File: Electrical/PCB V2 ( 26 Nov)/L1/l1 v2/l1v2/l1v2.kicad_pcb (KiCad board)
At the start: 2 copper layers, 177.9 x 169.6 mm, 157 parts, among them J1 Conn_01x01_Socket, J2 Conn_01x01_Socket, SW1 SW_SPDT, U1 ESP32-WROOM-32D-N4, U2 CD74HC4067SM, U3 CD74HC4067SM

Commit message: unfinished ocb with parts list
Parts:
- removed C22: 1uF, Capacitor_SMD:C_0603_1608Metric
- added C63: 1uF, Capacitor_SMD:C_0603_1608Metric, F.Cu at (164.0, 138.7)
- added L1: 10µH, Inductor_SMD:L_0805_2012Metric, F.Cu at (165.5, 116.1)
- added L33: 10µH, Inductor_SMD:L_0805_2012Metric, F.Cu at (166.1, 106.1)
- added L34: 10µH, Inductor_SMD:L_0805_2012Metric, F.Cu at (164.7, 96.2)
- added L35: 10µH, Inductor_SMD:L_0805_2012Metric, F.Cu at (161.4, 86.8)
- added L36: 10µH, Inductor_SMD:L_0805_2012Metric, F.Cu at (156.4, 78.2)
- added L37: 10µH, Inductor_SMD:L_0805_2012Metric, F.Cu at (149.7, 70.7)
- added L38: 10µH, Inductor_SMD:L_0805_2012Metric, F.Cu at (141.8, 64.7)
- added L39: 10µH, Inductor_SMD:L_0805_2012Metric, F.Cu at (132.8, 60.3)
- added L40: 10µH, Inductor_SMD:L_0805_2012Metric, F.Cu at (123.1, 57.8)
- added L41: 10µH, Inductor_SMD:L_0805_2012Metric, F.Cu at (113.1, 57.2)
- added L42: 10µH, Inductor_SMD:L_0805_2012Metric, F.Cu at (103.2, 58.6)
- added L43: 10µH, Inductor_SMD:L_0805_2012Metric, F.Cu at (93.8, 61.8)
- added L44: 10µH, Inductor_SMD:L_0805_2012Metric, F.Cu at (85.1, 66.9)
- added L45: 10µH, Inductor_SMD:L_0805_2012Metric, F.Cu at (77.7, 73.5)
- added L46: 10µH, Inductor_SMD:L_0805_2012Metric, F.Cu at (71.6, 81.5)
- added L47: 10µH, Inductor_SMD:L_0805_2012Metric, F.Cu at (67.3, 90.5)
- added L48: 10µH, Inductor_SMD:L_0805_2012Metric, F.Cu at (64.7, 100.2)
- added L49: 10µH, Inductor_SMD:L_0805_2012Metric, F.Cu at (64.2, 110.1)
- added L50: 10µH, Inductor_SMD:L_0805_2012Metric, F.Cu at (65.5, 120.0)
- added L51: 10µH, Inductor_SMD:L_0805_2012Metric, F.Cu at (68.8, 129.5)
- added L52: 10µH, Inductor_SMD:L_0805_2012Metric, F.Cu at (73.9, 138.1)
- added L53: 10µH, Inductor_SMD:L_0805_2012Metric, F.Cu at (80.5, 145.6)
- added L54: 10µH, Inductor_SMD:L_0805_2012Metric, F.Cu at (88.5, 151.6)
- added L55: 10µH, Inductor_SMD:L_0805_2012Metric, F.Cu at (97.5, 156.0)
- added L56: 10µH, Inductor_SMD:L_0805_2012Metric, F.Cu at (107.1, 158.5)
- added L57: 10µH, Inductor_SMD:L_0805_2012Metric, F.Cu at (117.1, 159.1)
- added L58: 10µH, Inductor_SMD:L_0805_2012Metric, F.Cu at (127.0, 157.7)
- added L59: 10µH, Inductor_SMD:L_0805_2012Metric, F.Cu at (136.5, 154.5)
- added L60: 10µH, Inductor_SMD:L_0805_2012Metric, F.Cu at (145.1, 149.4)
- added L61: 10µH, Inductor_SMD:L_0805_2012Metric, F.Cu at (152.6, 142.8)
- added L62: 10µH, Inductor_SMD:L_0805_2012Metric, F.Cu at (158.6, 134.8)
- added L63: 10µH, Inductor_SMD:L_0805_2012Metric, F.Cu at (163.0, 125.8)
- added LED10: WHITE 3528, LED_SMD:LED_PLCC_2835, F.Cu at (275.1, 145.3)
- added LED11: WHITE 3528, LED_SMD:LED_PLCC_2835, F.Cu at (264.8, 138.9)
- added LED12: WHITE 3528, LED_SMD:LED_PLCC_2835, F.Cu at (264.8, 140.6)
- added LED13: WHITE 3528, LED_SMD:LED_PLCC_2835, F.Cu at (264.8, 142.4)
- added LED14: WHITE 3528, LED_SMD:LED_PLCC_2835, F.Cu at (264.8, 144.1)
- added LED15: WHITE 3528, LED_SMD:LED_PLCC_2835, F.Cu at (264.8, 145.9)
- added LED16: WHITE 3528, LED_SMD:LED_PLCC_2835, F.Cu at (264.8, 147.6)
- added LED17: WHITE 3528, LED_SMD:LED_PLCC_2835, F.Cu at (264.8, 149.4)
- added LED18: WHITE 3528, LED_SMD:LED_PLCC_2835, F.Cu at (264.8, 151.1)
- added LED19: WHITE 3528, LED_SMD:LED_PLCC_2835, F.Cu at (267.5, 137.1)
- added LED2: WHITE 3528, LED_SMD:LED_PLCC_2835, F.Cu at (251.2, 153.7)
- added LED20: WHITE 3528, LED_SMD:LED_PLCC_2835, F.Cu at (267.5, 138.9)
- added LED21: WHITE 3528, LED_SMD:LED_PLCC_2835, F.Cu at (267.5, 140.6)
- added LED22: WHITE 3528, LED_SMD:LED_PLCC_2835, F.Cu at (267.5, 142.4)
- added LED23: WHITE 3528, LED_SMD:LED_PLCC_2835, F.Cu at (267.5, 144.1)
- added LED24: WHITE 3528, LED_SMD:LED_PLCC_2835, F.Cu at (267.5, 145.9)
- added LED25: WHITE 3528, LED_SMD:LED_PLCC_2835, F.Cu at (267.5, 147.6)
- added LED26: WHITE 3528, LED_SMD:LED_PLCC_2835, F.Cu at (267.5, 149.4)
- added LED27: WHITE 3528, LED_SMD:LED_PLCC_2835, F.Cu at (267.5, 151.1)
- added LED28: WHITE 3528, LED_SMD:LED_PLCC_2835, F.Cu at (270.2, 137.1)
- added LED29: WHITE 3528, LED_SMD:LED_PLCC_2835, F.Cu at (270.2, 138.9)
- added LED3: WHITE 3528, LED_SMD:LED_PLCC_2835, F.Cu at (262.1, 140.6)
- added LED30: WHITE 3528, LED_SMD:LED_PLCC_2835, F.Cu at (270.2, 140.6)
- added LED31: WHITE 3528, LED_SMD:LED_PLCC_2835, F.Cu at (270.2, 142.4)
- added LED32: WHITE 3528, LED_SMD:LED_PLCC_2835, F.Cu at (270.2, 144.1)
- added LED4: WHITE 3528, LED_SMD:LED_PLCC_2835, F.Cu at (262.1, 142.4)
- added LED5: WHITE 3528, LED_SMD:LED_PLCC_2835, F.Cu at (262.1, 144.1)
- added LED6: WHITE 3528, LED_SMD:LED_PLCC_2835, F.Cu at (262.1, 145.9)
- added LED7: WHITE 3528, LED_SMD:LED_PLCC_2835, F.Cu at (262.1, 147.6)
- added LED8: WHITE 3528, LED_SMD:LED_PLCC_2835, F.Cu at (262.1, 149.4)
- added LED9: WHITE 3528, LED_SMD:LED_PLCC_2835, F.Cu at (262.1, 151.1)
- H1, H10, H11, H12, H13, H14, H15, H16, H17, H18, H19, H2, H20, H21, H3, H4, H5, H6, H7, H8, H9: footprint MountingHole:MountingHole_3.2mm_M3 -> MountingHole:MountingHole_3.2mm_M3_DIN965_Pad
- LED1, LED33, LED34, LED35, LED36, LED37, LED38, LED39, LED40, LED41, LED42, LED43, LED44, LED45, LED46, LED47, LED48, LED49, LED50, LED51, LED52, LED53, LED54, LED55, LED56, LED57, LED58, LED59, LED60, LED61, LED62, LED63: footprint LED_SMD:LED_0201_0603Metric -> LED_SMD:LED_PLCC_2835
- LED_21: moved to F.Cu
- U1: value ESP32-WROOM-32D-N4 -> 102010428; footprint esp32 thinfy:MODULE_ESP32-WROOM-32D-N4 -> RF_Module:MCU_Seeed_ESP32C3
- moved LED_1 217.0 mm to (274.8, 77.5)
- moved LED_32 214.7 mm to (276.2, 132.7), turned to 0 degrees
- moved LED_31 210.7 mm to (276.2, 130.4), turned to 0 degrees
- moved LED_30 205.5 mm to (276.2, 128.0), turned to 0 degrees
- moved LED_2 203.1 mm to (263.1, 121.0), turned to 0 degrees
- moved LED_3 202.0 mm to (263.1, 123.3), turned to 0 degrees
- moved LED_4 199.6 mm to (263.1, 125.7), turned to 0 degrees
- moved LED_29 199.3 mm to (276.2, 125.7), turned to 0 degrees
- moved LED_5 196.0 mm to (263.1, 128.0), turned to 0 degrees
- moved LED_28 191.7 mm to (276.2, 123.3), turned to 0 degrees
- moved LED_6 191.3 mm to (263.1, 130.4), turned to 0 degrees
- moved LED_7 185.3 mm to (263.1, 132.7), turned to 0 degrees
- moved LED_27 183.4 mm to (276.2, 121.0), turned to 0 degrees
- moved LED_8 178.2 mm to (263.1, 135.1), turned to 0 degrees
- moved U2 174.8 mm to (255.4, 122.3)
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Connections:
- LED1 pad 1: GNDPWR -> GND
- LED33 pad 1: GNDPWR -> GND
- LED34 pad 1: GNDPWR -> GND
- LED35 pad 1: GNDPWR -> GND
- LED36 pad 1: GNDPWR -> GND
- LED37 pad 1: GNDPWR -> GND
- LED38 pad 1: GNDPWR -> GND
- LED39 pad 1: GNDPWR -> GND
- LED40 pad 1: GNDPWR -> GND
- LED41 pad 1: GNDPWR -> GND
- LED42 pad 1: GNDPWR -> GND
- LED43 pad 1: GNDPWR -> GND
- LED44 pad 1: GNDPWR -> GND
- LED45 pad 1: GNDPWR -> GND
- LED46 pad 1: GNDPWR -> GND
- LED47 pad 1: GNDPWR -> GND
- LED48 pad 1: GNDPWR -> GND
- LED49 pad 1: GNDPWR -> GND
- LED50 pad 1: GNDPWR -> GND
- LED51 pad 1: GNDPWR -> GND
- LED52 pad 1: GNDPWR -> GND
- LED53 pad 1: GNDPWR -> GND
- LED54 pad 1: GNDPWR -> GND
- LED55 pad 1: GNDPWR -> GND
- LED56 pad 1: GNDPWR -> GND
- LED57 pad 1: GNDPWR -> GND
- LED58 pad 1: GNDPWR -> GND
- LED59 pad 1: GNDPWR -> GND
- LED60 pad 1: GNDPWR -> GND
- LED61 pad 1: GNDPWR -> GND
- LED62 pad 1: GNDPWR -> GND
- LED63 pad 1: GNDPWR -> GND
- LED_17 pad 1: Net-(LED_1-Pad1) -> unconnected-(LED_17-Pad1)
- LED_18 pad 1: Net-(LED_1-Pad1) -> unconnected-(LED_17-Pad1)
- LED_19 pad 1: Net-(LED_1-Pad1) -> unconnected-(LED_17-Pad1)
- LED_20 pad 1: Net-(LED_1-Pad1) -> unconnected-(LED_17-Pad1)
- LED_21 pad 1: Net-(LED_1-Pad1) -> unconnected-(LED_17-Pad1)
- LED_22 pad 1: Net-(LED_1-Pad1) -> unconnected-(LED_17-Pad1)
- LED_23 pad 1: Net-(LED_1-Pad1) -> unconnected-(LED_17-Pad1)
- LED_24 pad 1: Net-(LED_1-Pad1) -> unconnected-(LED_17-Pad1)
- LED_25 pad 1: Net-(LED_1-Pad1) -> unconnected-(LED_17-Pad1)
- LED_26 pad 1: Net-(LED_1-Pad1) -> unconnected-(LED_17-Pad1)
- LED_27 pad 1: Net-(LED_1-Pad1) -> unconnected-(LED_17-Pad1)
- LED_28 pad 1: Net-(LED_1-Pad1) -> unconnected-(LED_17-Pad1)
- LED_29 pad 1: Net-(LED_1-Pad1) -> unconnected-(LED_17-Pad1)
- LED_30 pad 1: Net-(LED_1-Pad1) -> unconnected-(LED_17-Pad1)
- LED_31 pad 1: Net-(LED_1-Pad1) -> unconnected-(LED_17-Pad1)
- LED_32 pad 1: Net-(LED_1-Pad1) -> unconnected-(LED_17-Pad1)
- TP2 pad 1: GNDPWR -> GND
- U1 pad 1: Net-(U1-GND-Pad1) -> unconnected-(U1-P26/A0/D0-Pad1)
- U1 pad 11: Net-(U1-IO26) -> unconnected-(U1-D10/MOSI/P3-Pad11)
- U1 pad 12: Net-(U1-IO27) -> 3v3
- U1 pad 13: unconnected-(U1-IO14-Pad13) -> GND
- U1 pad 15: Net-(U1-GND-Pad1) -> (no net)
- U1 pad 16: unconnected-(U1-IO13-Pad16) -> (no net)
- U1 pad 17: unconnected-(U1-SHD/SD2-Pad17) -> (no net)
- U1 pad 18: unconnected-(U1-SWP/SD3-Pad18) -> (no net)
- U1 pad 19: unconnected-(U1-SCS/CMD-Pad19) -> (no net)
- U1 pad 2: 3V3 -> unconnected-(U1-P27/A1/D1-Pad2)
- U1 pad 20: unconnected-(U1-SCK/CLK-Pad20) -> (no net)
- U1 pad 21: unconnected-(U1-SDO/SD0-Pad21) -> (no net)
- U1 pad 22: unconnected-(U1-SDI/SD1-Pad22) -> (no net)
- U1 pad 23: unconnected-(U1-IO15-Pad23) -> (no net)
- U1 pad 8: Net-(U1-IO32) -> unconnected-(U1-D7/CSB/P1/RX-Pad8)
- U1 pad 9: Net-(U1-IO33) -> unconnected-(U1-D8/SCK/P2-Pad9)
- U2 pad 1: Net-(U1-RXD0) -> unconnected-(U2-COM-Pad1)
- U2 pad 10: Net-(U1-IO26) -> unconnected-(U2-S0-Pad10)
- U2 pad 11: Net-(U1-IO27) -> unconnected-(U2-S1-Pad11)
- U2 pad 13: Net-(U1-IO33) -> unconnected-(U2-S3-Pad13)
- U2 pad 14: Net-(U1-IO32) -> unconnected-(U2-S2-Pad14)
- U3 pad 1: Net-(U1-RXD0) -> unconnected-(U3-COM-Pad1)
- U3 pad 10: Net-(U1-IO0) -> unconnected-(U3-S0-Pad10)
- U3 pad 11: Net-(U1-IO21) -> unconnected-(U3-S1-Pad11)
- U3 pad 13: Net-(U1-IO23) -> unconnected-(U3-S3-Pad13)
- U3 pad 14: Net-(U1-IO22) -> unconnected-(U3-S2-Pad14)
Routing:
- net GNDPWR: track 759.6 -> 10.1 mm
- net pwr for photoresistors: track 24.2 -> 0.00 mm, vias 1 -> 0
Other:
- board text removed: "2 Chairs"
- board text removed: "Just Better."
- board text removed: "两张椅子 比你好"

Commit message: wireed photoresistors for l1
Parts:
- removed C33, C34, C35, C36, C37, C38, C39, C40, C41, C42, C43, C44, C45, C46, C47, C48, C49, C50, C51, C52, C53, C54, C55, C56, C57, C58, C59, C60, C61, C62, C63: 1uF, Capacitor_SMD:C_0603_1608Metric
- removed L33, L34, L35, L36, L37, L38, L39, L40, L41, L42, L43, L44, L45, L46, L47, L48, L49, L50, L51, L52, L53, L54, L55, L56, L57, L58, L59, L60, L61, L62, L63: 10µH, Inductor_SMD:L_0805_2012Metric
- removed LED33, LED34, LED35, LED36, LED37, LED38, LED39, LED40, LED41, LED42, LED43, LED44, LED45, LED46, LED47, LED48, LED49, LED50, LED51, LED52, LED53, LED54, LED55, LED56, LED57, LED58, LED59, LED60, LED61, LED62, LED63: WHITE 3528, LED_SMD:LED_PLCC_2835
- removed LED_1: R_Photo, photoresistor:XDCR_ALS-PT19-315C_L177_TR8
- removed R33, R34, R35, R36, R37, R38, R39, R40, R41, R42, R43, R44, R45, R46, R47, R48, R49, R50, R51, R52, R53, R54, R55, R56, R57, R58, R59, R60, R61, R62, R63: 0R39, Resistor_SMD:R_0603_1608Metric
- added C10: 1uF, Capacitor_SMD:C_0603_1608Metric, B.Cu at (129.5, 166.1)
- added C11: 1uF, Capacitor_SMD:C_0603_1608Metric, B.Cu at (140.2, 162.6)
- added C12: 1uF, Capacitor_SMD:C_0603_1608Metric, B.Cu at (150.1, 157.1)
- added C13: 1uF, Capacitor_SMD:C_0603_1608Metric, B.Cu at (158.7, 149.7)
- added C14: 1uF, Capacitor_SMD:C_0603_1608Metric, B.Cu at (165.7, 140.8)
- added C15: 1uF, Capacitor_SMD:C_0603_1608Metric, B.Cu at (170.8, 130.7)
- added C16: 1uF, Capacitor_SMD:C_0603_1608Metric, B.Cu at (173.8, 119.8)
- added C17: 1uF, Capacitor_SMD:C_0603_1608Metric, B.Cu at (174.7, 108.6)
- added C18: 1uF, Capacitor_SMD:C_0603_1608Metric, B.Cu at (173.3, 97.3)
- added C19: 1uF, Capacitor_SMD:C_0603_1608Metric, B.Cu at (169.8, 86.6)
- added C2: 1uF, Capacitor_SMD:C_0603_1608Metric, B.Cu at (60.7, 122.3)
- added C20: 1uF, Capacitor_SMD:C_0603_1608Metric, B.Cu at (164.2, 76.8)
- added C21: 1uF, Capacitor_SMD:C_0603_1608Metric, B.Cu at (156.9, 68.2)
- added C22: 1uF, Capacitor_SMD:C_0603_1608Metric, B.Cu at (148.0, 61.2)
- added C23: 1uF, Capacitor_SMD:C_0603_1608Metric, B.Cu at (137.9, 56.1)
- added C24: 1uF, Capacitor_SMD:C_0603_1608Metric, B.Cu at (127.0, 53.0)
- added C25: 1uF, Capacitor_SMD:C_0603_1608Metric, B.Cu at (115.7, 52.2)
- added C26: 1uF, Capacitor_SMD:C_0603_1608Metric, B.Cu at (104.5, 53.5)
- added C27: 1uF, Capacitor_SMD:C_0603_1608Metric, B.Cu at (93.8, 57.1)
- added C28: 1uF, Capacitor_SMD:C_0603_1608Metric, B.Cu at (83.9, 62.6)
- added C29: 1uF, Capacitor_SMD:C_0603_1608Metric, B.Cu at (75.3, 70.0)
- added C3: 1uF, Capacitor_SMD:C_0603_1608Metric, B.Cu at (64.2, 133.1)
- added C30: 1uF, Capacitor_SMD:C_0603_1608Metric, B.Cu at (68.4, 78.9)
- added C31: 1uF, Capacitor_SMD:C_0603_1608Metric, B.Cu at (63.2, 88.9)
- added C32: 1uF, Capacitor_SMD:C_0603_1608Metric, B.Cu at (60.2, 99.8)
- added C4: 1uF, Capacitor_SMD:C_0603_1608Metric, B.Cu at (69.8, 142.9)
- added C5: 1uF, Capacitor_SMD:C_0603_1608Metric, B.Cu at (77.1, 151.5)
- added C6: 1uF, Capacitor_SMD:C_0603_1608Metric, B.Cu at (86.0, 158.5)
- added C7: 1uF, Capacitor_SMD:C_0603_1608Metric, B.Cu at (96.1, 163.6)
- added C8: 1uF, Capacitor_SMD:C_0603_1608Metric, B.Cu at (107.0, 166.6)
- added C9: 1uF, Capacitor_SMD:C_0603_1608Metric, B.Cu at (118.3, 167.5)
- added L10: 10µH, Inductor_SMD:L_0805_2012Metric, B.Cu at (125.0, 162.9)
- added L11: 10µH, Inductor_SMD:L_0805_2012Metric, B.Cu at (135.2, 160.3)
- added L12: 10µH, Inductor_SMD:L_0805_2012Metric, B.Cu at (144.7, 155.8)
- added L13: 10µH, Inductor_SMD:L_0805_2012Metric, B.Cu at (153.2, 149.5)
- added L14: 10µH, Inductor_SMD:L_0805_2012Metric, B.Cu at (160.2, 141.7)
- added L15: 10µH, Inductor_SMD:L_0805_2012Metric, B.Cu at (165.6, 132.7)
- added L16: 10µH, Inductor_SMD:L_0805_2012Metric, B.Cu at (169.1, 122.7)
- added L17: 10µH, Inductor_SMD:L_0805_2012Metric, B.Cu at (170.6, 112.3)
- added L18: 10µH, Inductor_SMD:L_0805_2012Metric, B.Cu at (170.1, 101.8)
- added L19: 10µH, Inductor_SMD:L_0805_2012Metric, B.Cu at (167.5, 91.6)
- added L2: 10µH, Inductor_SMD:L_0805_2012Metric, B.Cu at (63.9, 117.9)
- added L20: 10µH, Inductor_SMD:L_0805_2012Metric, B.Cu at (163.0, 82.1)
- added L21: 10µH, Inductor_SMD:L_0805_2012Metric, B.Cu at (156.7, 73.7)
- added L22: 10µH, Inductor_SMD:L_0805_2012Metric, B.Cu at (148.9, 66.6)
- added L23: 10µH, Inductor_SMD:L_0805_2012Metric, B.Cu at (139.8, 61.2)
- added L24: 10µH, Inductor_SMD:L_0805_2012Metric, B.Cu at (129.9, 57.7)
- added L25: 10µH, Inductor_SMD:L_0805_2012Metric, B.Cu at (119.5, 56.2)
- added L26: 10µH, Inductor_SMD:L_0805_2012Metric, B.Cu at (109.0, 56.8)
- added L27: 10µH, Inductor_SMD:L_0805_2012Metric, B.Cu at (98.8, 59.3)
- added L28: 10µH, Inductor_SMD:L_0805_2012Metric, B.Cu at (89.3, 63.9)
- added L29: 10µH, Inductor_SMD:L_0805_2012Metric, B.Cu at (80.8, 70.2)
- added L3: 10µH, Inductor_SMD:L_0805_2012Metric, B.Cu at (66.5, 128.1)
- added L30: 10µH, Inductor_SMD:L_0805_2012Metric, B.Cu at (73.8, 78.0)
- added L31: 10µH, Inductor_SMD:L_0805_2012Metric, B.Cu at (68.4, 87.0)
- added L32: 10µH, Inductor_SMD:L_0805_2012Metric, B.Cu at (64.9, 96.9)
- added L4: 10µH, Inductor_SMD:L_0805_2012Metric, B.Cu at (71.0, 137.6)
- added L5: 10µH, Inductor_SMD:L_0805_2012Metric, B.Cu at (77.3, 146.0)
- added L6: 10µH, Inductor_SMD:L_0805_2012Metric, B.Cu at (85.2, 153.0)
- added L7: 10µH, Inductor_SMD:L_0805_2012Metric, B.Cu at (94.2, 158.4)
- added L8: 10µH, Inductor_SMD:L_0805_2012Metric, B.Cu at (104.1, 161.9)
- added L9: 10µH, Inductor_SMD:L_0805_2012Metric, B.Cu at (114.5, 163.5)
- added LED_33: R_Photo, photoresistor:XDCR_ALS-PT19-315C_L177_TR8, B.Cu at (62.7, 101.8)
- added R10: 0R39, Resistor_SMD:R_0603_1608Metric, B.Cu at (125.8, 166.2)
- added R11: 0R39, Resistor_SMD:R_0603_1608Metric, B.Cu at (136.6, 163.4)
- added R12: 0R39, Resistor_SMD:R_0603_1608Metric, B.Cu at (146.7, 158.6)
- added R13: 0R39, Resistor_SMD:R_0603_1608Metric, B.Cu at (155.6, 151.8)
- added R14: 0R39, Resistor_SMD:R_0603_1608Metric, B.Cu at (163.1, 143.5)
- added R15: 0R39, Resistor_SMD:R_0603_1608Metric, B.Cu at (168.8, 133.9)
- added R16: 0R39, Resistor_SMD:R_0603_1608Metric, B.Cu at (172.5, 123.3)
- added R17: 0R39, Resistor_SMD:R_0603_1608Metric, B.Cu at (174.0, 112.2)
- added R18: 0R39, Resistor_SMD:R_0603_1608Metric, B.Cu at (173.4, 101.1)
- added R19: 0R39, Resistor_SMD:R_0603_1608Metric, B.Cu at (170.6, 90.2)
- added R2: 0R39, Resistor_SMD:R_0603_1608Metric, B.Cu at (60.6, 118.6)
- added R20: 0R39, Resistor_SMD:R_0603_1608Metric, B.Cu at (165.7, 80.2)
- added R21: 0R39, Resistor_SMD:R_0603_1608Metric, B.Cu at (159.0, 71.2)
- added R22: 0R39, Resistor_SMD:R_0603_1608Metric, B.Cu at (150.7, 63.8)
- added R23: 0R39, Resistor_SMD:R_0603_1608Metric, B.Cu at (141.0, 58.1)
- added R24: 0R39, Resistor_SMD:R_0603_1608Metric, B.Cu at (130.5, 54.4)
- added R25: 0R39, Resistor_SMD:R_0603_1608Metric, B.Cu at (119.4, 52.8)
- added R26: 0R39, Resistor_SMD:R_0603_1608Metric, B.Cu at (108.2, 53.5)
- added R27: 0R39, Resistor_SMD:R_0603_1608Metric, B.Cu at (97.4, 56.3)
- added R28: 0R39, Resistor_SMD:R_0603_1608Metric, B.Cu at (87.3, 61.1)
- added R29: 0R39, Resistor_SMD:R_0603_1608Metric, B.Cu at (78.4, 67.8)
- added R3: 0R39, Resistor_SMD:R_0603_1608Metric, B.Cu at (63.4, 129.4)
- added R30: 0R39, Resistor_SMD:R_0603_1608Metric, B.Cu at (70.9, 76.2)
- added R31: 0R39, Resistor_SMD:R_0603_1608Metric, B.Cu at (65.3, 85.8)
- added R32: 0R39, Resistor_SMD:R_0603_1608Metric, B.Cu at (61.6, 96.4)
- added R4: 0R39, Resistor_SMD:R_0603_1608Metric, B.Cu at (68.3, 139.5)
- added R5: 0R39, Resistor_SMD:R_0603_1608Metric, B.Cu at (75.0, 148.5)
- added R6: 0R39, Resistor_SMD:R_0603_1608Metric, B.Cu at (83.3, 155.9)
- added R7: 0R39, Resistor_SMD:R_0603_1608Metric, B.Cu at (93.0, 161.6)
- added R8: 0R39, Resistor_SMD:R_0603_1608Metric, B.Cu at (103.5, 165.3)
- added R9: 0R39, Resistor_SMD:R_0603_1608Metric, B.Cu at (114.6, 166.9)
- C1, L1, LED1, LED10, LED11, LED12, LED13, LED14, LED15, LED16, LED17, LED18, LED19, LED2, LED20, LED21, LED22, LED23, LED24, LED25, LED26, LED27, LED28, LED29, LED3, LED30, LED31, LED32, LED4, LED5, LED6, LED7, LED8, LED9, LED_10, LED_11, LED_12, LED_13, LED_14, LED_15, LED_16, LED_17, LED_18, LED_19, LED_2, LED_20, LED_21, LED_22, LED_23, LED_24, LED_25, LED_26, LED_27, LED_28, LED_29, LED_3, LED_30, LED_31, LED_32, LED_4, LED_5, LED_6, LED_7, LED_8, LED_9, R1, U2, U3: moved to B.Cu
- moved H8 266.3 mm to (93.7, 175.6)
- moved H13 241.8 mm to (141.1, 175.4)
- moved H21 233.2 mm to (84.7, 118.0)
- moved H17 217.4 mm to (84.1, 98.6)
- moved LED_32 214.9 mm to (65.3, 91.4), turned to 157.5 degrees
- moved H12 212.5 mm to (78.9, 93.3)
- moved LED_31 212.0 mm to (69.9, 81.7), turned to 146.25 degrees
- moved LED32 211.5 mm to (63.5, 99.4), turned to 168.75 degrees
- moved LED31 210.5 mm to (66.5, 89.2), turned to 157.5 degrees
- moved LED30 207.8 mm to (71.5, 79.7), turned to 146.25 degrees
- moved LED_30 207.3 mm to (76.3, 73.0), turned to 135 degrees
- moved LED29 203.4 mm to (78.3, 71.5), turned to 135 degrees
- moved LED_2 201.1 mm to (62.2, 112.6), turned to 180 degrees
- moved LED_29 201.1 mm to (84.3, 65.8), turned to 123.75 degrees
- moved H20 200.2 mm to (101.3, 70.2)
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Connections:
- LED_10 pad 1: Net-(LED_1-Pad1) -> 3v3
- LED_11 pad 1: Net-(LED_1-Pad1) -> 3v3
- LED_12 pad 1: Net-(LED_1-Pad1) -> 3v3
- LED_13 pad 1: Net-(LED_1-Pad1) -> 3v3
- LED_14 pad 1: Net-(LED_1-Pad1) -> 3v3
- LED_15 pad 1: Net-(LED_1-Pad1) -> 3v3
- LED_16 pad 1: Net-(LED_1-Pad1) -> 3v3
- LED_17 pad 1: unconnected-(LED_17-Pad1) -> 3v3
- LED_18 pad 1: unconnected-(LED_17-Pad1) -> 3v3
- LED_19 pad 1: unconnected-(LED_17-Pad1) -> 3v3
- LED_2 pad 1: Net-(LED_1-Pad1) -> 3v3
- LED_2 pad 2: Net-(U2-I1) -> Net-(U2-I2)
- LED_20 pad 1: unconnected-(LED_17-Pad1) -> 3v3
- LED_21 pad 1: unconnected-(LED_17-Pad1) -> 3v3
- LED_22 pad 1: unconnected-(LED_17-Pad1) -> 3v3
- LED_23 pad 1: unconnected-(LED_17-Pad1) -> 3v3
- LED_24 pad 1: unconnected-(LED_17-Pad1) -> 3v3
- LED_25 pad 1: unconnected-(LED_17-Pad1) -> 3v3
- LED_26 pad 1: unconnected-(LED_17-Pad1) -> 3v3
- LED_27 pad 1: unconnected-(LED_17-Pad1) -> 3v3
- LED_28 pad 1: unconnected-(LED_17-Pad1) -> 3v3
- LED_29 pad 1: unconnected-(LED_17-Pad1) -> 3v3
- LED_3 pad 1: Net-(LED_1-Pad1) -> 3v3
- LED_3 pad 2: Net-(U2-I2) -> Net-(U2-I1)
- LED_30 pad 1: unconnected-(LED_17-Pad1) -> 3v3
- LED_31 pad 1: unconnected-(LED_17-Pad1) -> 3v3
- LED_32 pad 1: unconnected-(LED_17-Pad1) -> 3v3
- LED_4 pad 1: Net-(LED_1-Pad1) -> 3v3
- LED_4 pad 2: Net-(U2-I3) -> Net-(U2-I6)
- LED_5 pad 1: Net-(LED_1-Pad1) -> 3v3
- LED_5 pad 2: Net-(U2-I4) -> Net-(U2-I5)
- LED_6 pad 1: Net-(LED_1-Pad1) -> 3v3
- LED_6 pad 2: Net-(U2-I5) -> Net-(U2-I4)
- LED_7 pad 1: Net-(LED_1-Pad1) -> 3v3
- LED_7 pad 2: Net-(U2-I6) -> Net-(U2-I3)
- LED_8 pad 1: Net-(LED_1-Pad1) -> 3v3
- LED_9 pad 1: Net-(LED_1-Pad1) -> 3v3
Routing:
- net pwr for photoresistors: track 0.00 -> 94.6 mm
- net Net-(U3-I14): track 0.00 -> 67.1 mm
- net Net-(U3-I10): track 0.00 -> 66.6 mm
- net Net-(U2-I3): track 0.00 -> 66.2 mm
- net Net-(U2-I1): track 0.00 -> 65.6 mm, vias 0 -> 2
- net Net-(U2-I7): track 0.00 -> 62.5 mm
- net Net-(U2-I2): track 0.00 -> 62.0 mm
- net Net-(U2-I15): track 0.00 -> 61.4 mm
- net Net-(U2-I11): track 0.00 -> 60.9 mm
- net Net-(U2-I6): track 0.00 -> 60.4 mm, vias 0 -> 2
- net Net-(U3-I11): track 0.00 -> 59.6 mm
- net Net-(U2-I14): track 0.00 -> 59.1 mm
- net Net-(U2-I5): track 0.00 -> 58.9 mm, vias 0 -> 2
- net Net-(U2-I12): track 0.00 -> 58.4 mm
- net Net-(U2-I4): track 0.00 -> 58.2 mm, vias 0 -> 2
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
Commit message: did led wiring to 3v3 and to muxes.
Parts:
- removed LED_33: R_Photo, photoresistor:XDCR_ALS-PT19-315C_L177_TR8
- added H22: MountingHole, MountingHole:MountingHole_3.2mm_M3_DIN965_Pad, F.Cu at (132.8, 147.1)
- added H23: MountingHole, MountingHole:MountingHole_3.2mm_M3_DIN965_Pad, F.Cu at (93.9, 170.3)
- added H24: MountingHole, MountingHole:MountingHole_3.2mm_M3_DIN965_Pad, F.Cu at (140.8, 170.3)
- added LED_1: R_Photo, photoresistor:XDCR_ALS-PT19-315C_L177_TR8, B.Cu at (63.7, 100.3)
- moved TP1 208.5 mm to (97.6, 27.1)
- moved TP2 207.0 mm to (102.9, 27.1)
- moved SW1 132.0 mm to (133.8, 26.7), turned to 90 degrees
- moved H2 126.3 mm to (142.4, 29.5)
- moved J1 122.1 mm to (137.2, 38.7)
- moved J2 117.0 mm to (141.3, 37.2)
- moved H6 114.1 mm to (196.3, 83.5)
- moved H9 113.9 mm to (78.8, 93.1)
- moved H8 105.1 mm to (126.8, 75.9)
- moved H1 95.6 mm to (92.3, 29.5)
- moved H5 95.2 mm to (38.3, 83.5)
- moved H15 90.2 mm to (38.4, 133.5)
- moved H16 88.8 mm to (196.3, 133.5)
- moved H13 80.5 mm to (84.7, 118.0)
- moved H3 75.5 mm to (101.9, 70.0)
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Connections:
- C1 pad 2: GNDPWR -> GND
- C10 pad 2: GNDPWR -> GND
- C11 pad 2: GNDPWR -> GND
- C12 pad 2: GNDPWR -> GND
- C13 pad 2: GNDPWR -> GND
- C14 pad 2: GNDPWR -> GND
- C15 pad 2: GNDPWR -> GND
- C16 pad 2: GNDPWR -> GND
- C17 pad 2: GNDPWR -> GND
- C18 pad 2: GNDPWR -> GND
- C19 pad 2: GNDPWR -> GND
- C2 pad 2: GNDPWR -> GND
- C20 pad 2: GNDPWR -> GND
- C21 pad 2: GNDPWR -> GND
- C22 pad 2: GNDPWR -> GND
- C23 pad 2: GNDPWR -> GND
- C24 pad 2: GNDPWR -> GND
- C25 pad 2: GNDPWR -> GND
- C26 pad 2: GNDPWR -> GND
- C27 pad 2: GNDPWR -> GND
- C28 pad 2: GNDPWR -> GND
- C29 pad 2: GNDPWR -> GND
- C3 pad 2: GNDPWR -> GND
- C30 pad 2: GNDPWR -> GND
- C31 pad 2: GNDPWR -> GND
- C32 pad 2: GNDPWR -> GND
- C4 pad 2: GNDPWR -> GND
- C5 pad 2: GNDPWR -> GND
- C6 pad 2: GNDPWR -> GND
- C7 pad 2: GNDPWR -> GND
- C8 pad 2: GNDPWR -> GND
- C9 pad 2: GNDPWR -> GND
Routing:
- net 3v3: track 0.00 -> 511.2 mm, vias 0 -> 2
- net Net-(U2-I0): track 0.00 -> 60.5 mm
- net Net-(U2-I10): track 54.7 -> 49.9 mm
- net Net-(U2-I12): track 58.4 -> 53.8 mm
- net Net-(U2-I15): track 61.4 -> 56.9 mm
- net Net-(U3-I4): track 53.3 -> 49.2 mm
- net Net-(U2-I9): track 51.5 -> 47.3 mm
- net Net-(U2-I11): track 60.9 -> 57.2 mm
- net Net-(U2-I13): track 57.5 -> 53.9 mm
- net Net-(U3-I2): track 53.8 -> 50.4 mm
- net Net-(U3-I5): track 56.8 -> 53.5 mm
- net Net-(U2-I1): track 65.6 -> 62.3 mm
- net Net-(U2-I14): track 59.1 -> 56.1 mm
- net Net-(U2-I2): track 62.0 -> 59.5 mm
- net Net-(U2-I6): track 60.4 -> 57.9 mm
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- added copper zone on B.Cu, net GND
- added copper zone on F.Cu, net GND
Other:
- board text added: "3v3"
- board text added: "GND"
- board text added: "Led Power Test"

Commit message: did pwr wiring to some extent
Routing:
- net pwr for photoresistors: track 94.6 -> 575.0 mm, vias 0 -> 32

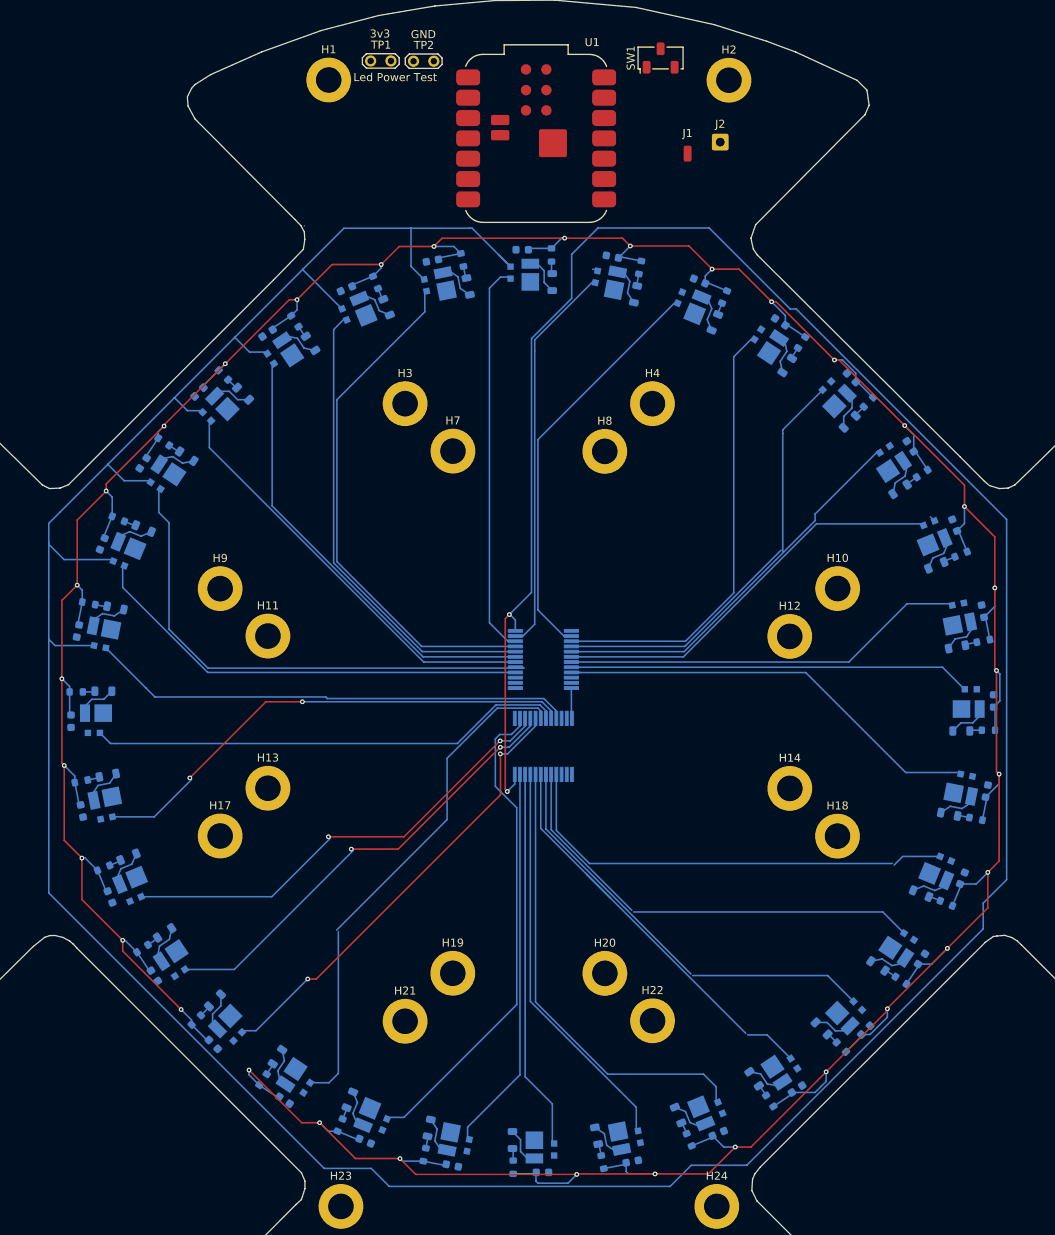
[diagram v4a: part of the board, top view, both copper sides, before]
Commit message: added l2 dxf, did some more stuff to l1
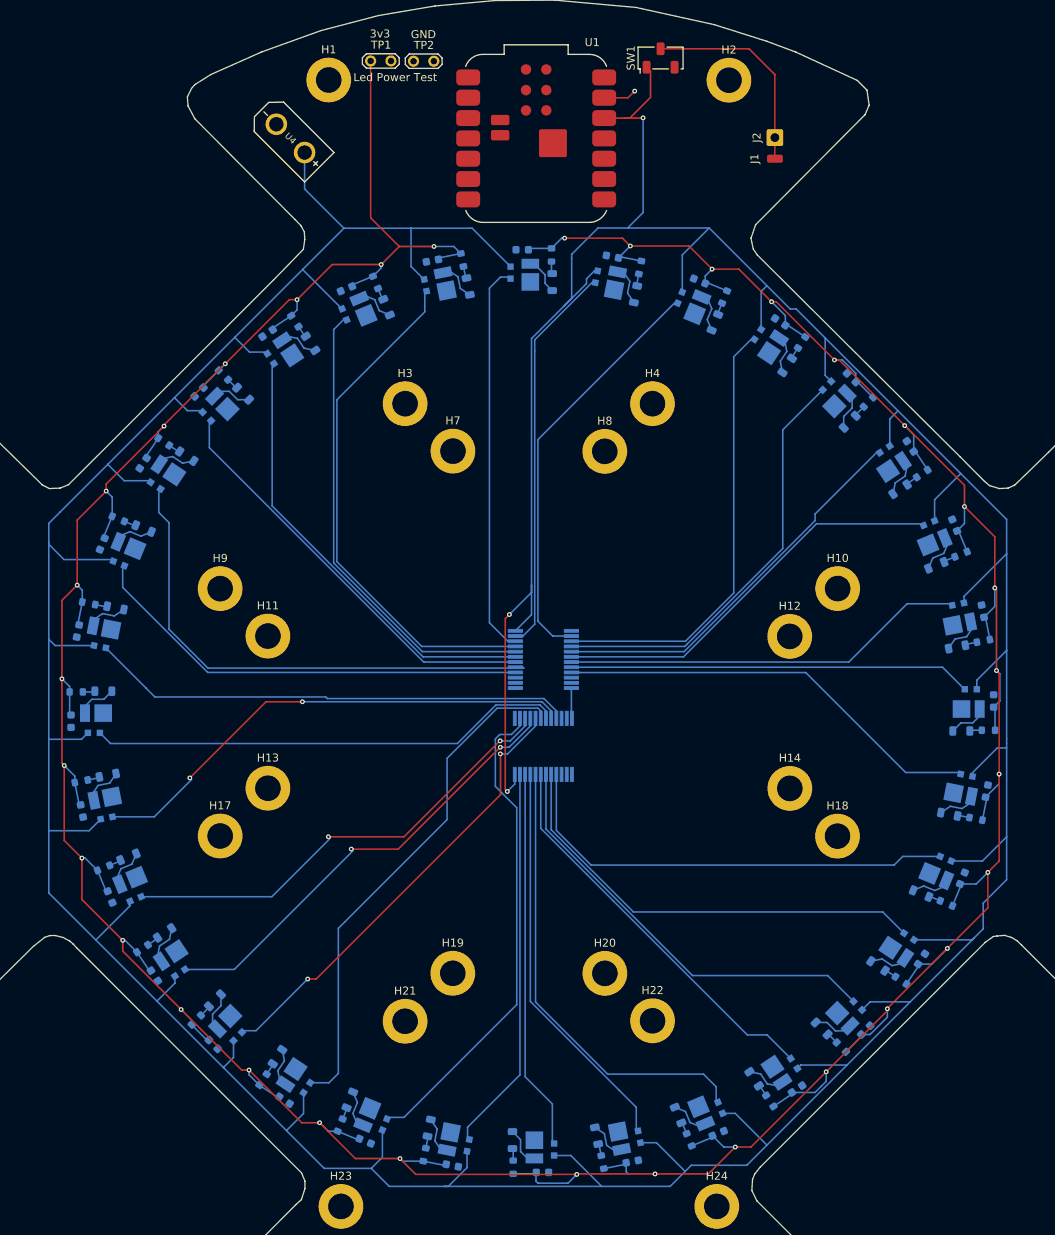
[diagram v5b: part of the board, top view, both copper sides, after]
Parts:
- added U4: XT30UPB-M, xt30-m:XT30UPB-M, F.Cu at (87.5, 36.8)
- moved J1 10.9 mm to (148.1, 39.3), turned to 90 degrees
- moved J2 6.85 mm to (148.1, 36.7), turned to 90 degrees
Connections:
- SW1 pad 1: 3V3 -> 3v3
- U2 pad 10: unconnected-(U2-S0-Pad10) -> /Mux 1 
- U2 pad 11: unconnected-(U2-S1-Pad11) -> /Mux 2
- U2 pad 13: unconnected-(U2-S3-Pad13) -> /Mux 4
- U2 pad 14: unconnected-(U2-S2-Pad14) -> /Mux 3
- U3 pad 10: unconnected-(U3-S0-Pad10) -> /Mux 8
- U3 pad 11: unconnected-(U3-S1-Pad11) -> /Mux 7
- U3 pad 13: unconnected-(U3-S3-Pad13) -> /Mux 5
- U3 pad 14: unconnected-(U3-S2-Pad14) -> /Mux 6
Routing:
- net 3v3: track 511.2 -> 706.5 mm, vias 2 -> 3
- net pwr for photoresistors: track 575.0 -> 620.7 mm
- net GND: track 3.82 -> 7.98 mm, vias 0 -> 1
- net Net-(U2-I12): track 53.8 -> 49.9 mm
- net Net-(U3-I7): track 51.2 -> 52.0 mm
